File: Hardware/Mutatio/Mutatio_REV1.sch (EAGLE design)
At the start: 41 parts, among them IC1 OPA743, IC2 74AUC1G14DBV, IC3 MCP1703CB, J1 MICRO-SDCARD-CONNECTOR-330006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

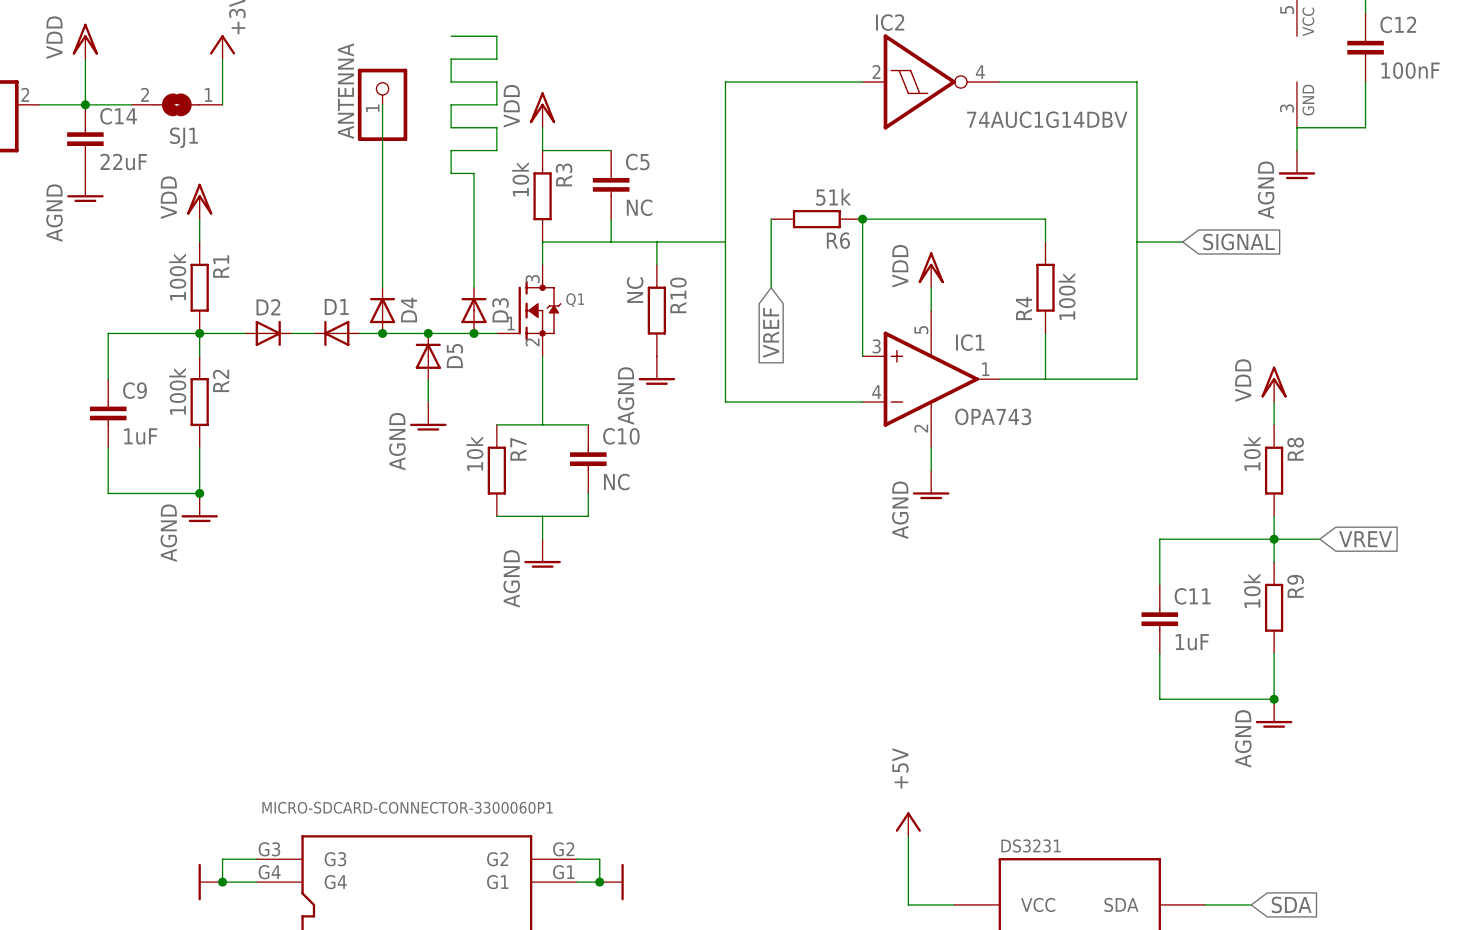
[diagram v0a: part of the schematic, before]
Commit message: Added bug description and changed component values
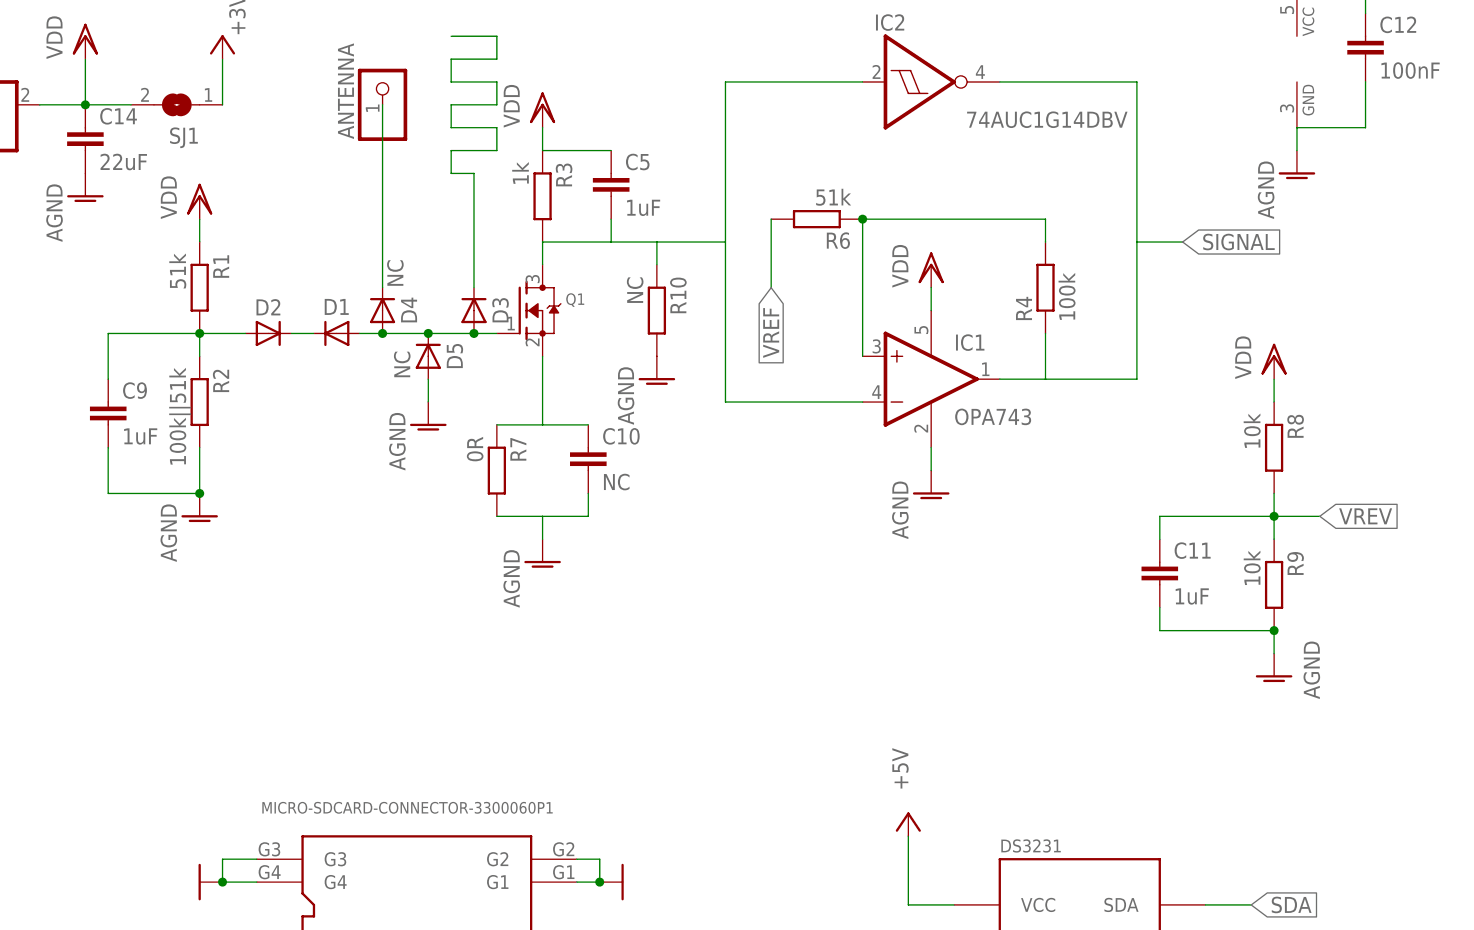
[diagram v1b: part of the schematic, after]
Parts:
- C5: value NC -> 1uF
- D4, D5: value (none) -> NC
- R1: value 100k -> 51k
- R2: value 100k -> 100k||51k
- R3: value 10k -> 1k
- R7: value 10k -> 0R
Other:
- note added: "CONNECT"
- note added: "For high noise supply: add 220R resistor here (filter 5V noise for analog circuit)"
- note added: "NC"
- note added: "OPAMP SCHMITT TRIGGER USE INSTEAD OF SCHMITT TRIGGER OR DO NOT PLACE"
- note added: "Solder Jumperwire (hardware bug)"
- note added: "Switch 'Signal' with 'WS8212_DIN' (hardware bug)"
- moved on the sheet: C11, R8, R9

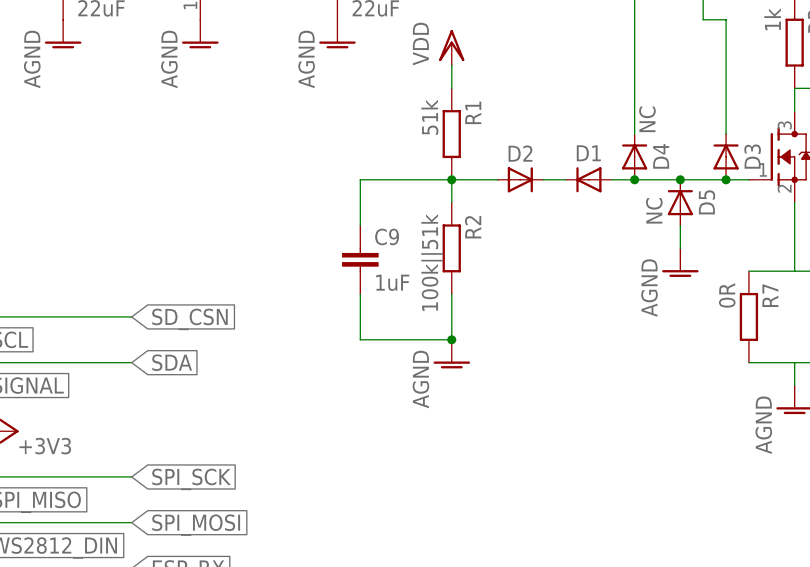
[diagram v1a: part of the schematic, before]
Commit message: Added bug description and changed component values
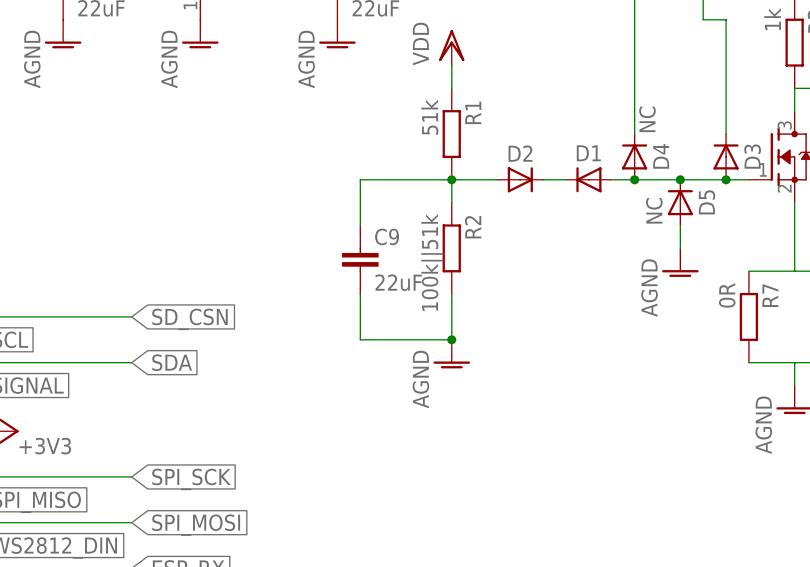
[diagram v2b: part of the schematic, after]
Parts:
- C9: value 1uF -> 22uF
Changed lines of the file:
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@@
 <part name="D1" library="diode" deviceset="DIODE-" device="MINIMELF"/>
 <part name="U$1" library="DS3231_Module" deviceset="DS3231_MODULE" device="BIG_CONNECTER_ONLY"/>
-<part name="C9" library="resistor" deviceset="C-EU" device="C0603" value="1uF"/>
+<part name="C9" library="resistor" deviceset="C-EU" device="C0603" value="22uF"/>
 <part name="R1" library="resistor" deviceset="R-EU_" device="R0603" value="51k"/>
 <part name="R2" library="resistor" deviceset="R-EU_" device="R0603" value="100k||51k"/>
